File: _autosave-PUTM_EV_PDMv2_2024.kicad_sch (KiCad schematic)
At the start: 11 parts, among them J5 FTSH-107-01-L-DV-K-A, J6 USB_B_Micro, J7 USB_C_Receptacle_USB2.0_14P, U1 STM32G0C1KCTxN

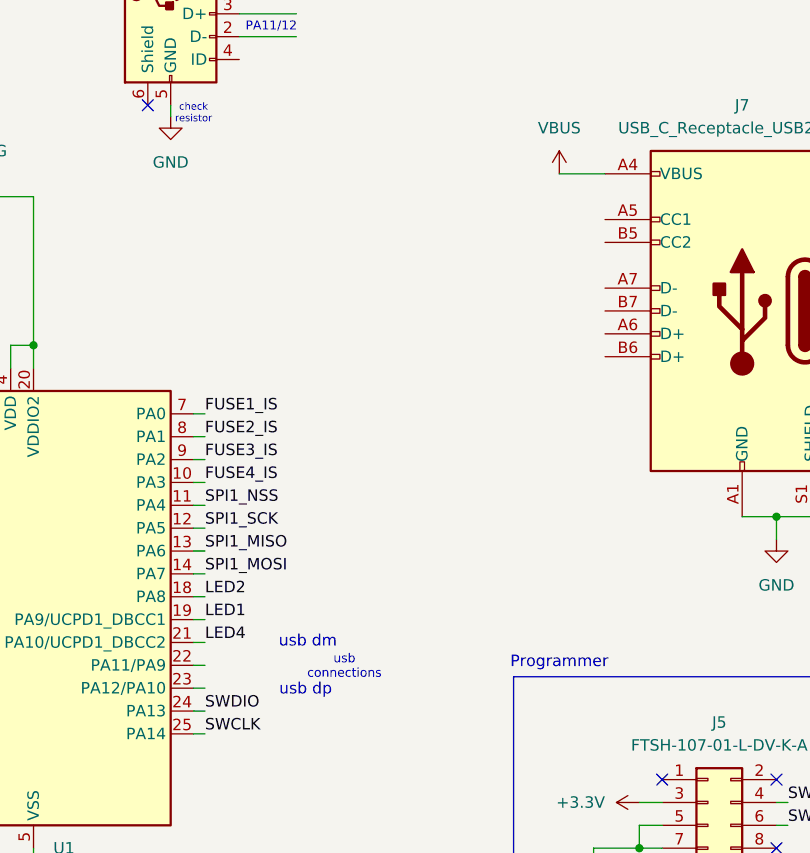
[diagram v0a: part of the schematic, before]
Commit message: Finished schematic
Added UCB C connection
Added CAN
Power ICs schematic fixed
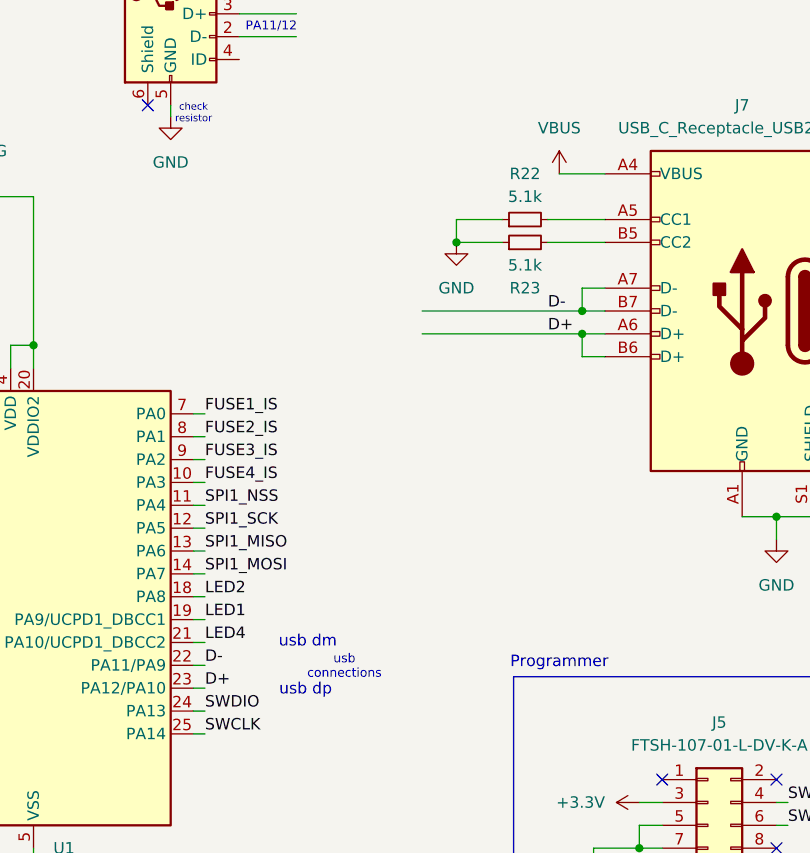
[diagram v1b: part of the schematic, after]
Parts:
- added R22, R23: 5.1k, symbol Device:R_Small
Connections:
- net GND: now also R22.1, R23.1
- net at J7.A5 (CC1): now also R22.2
- net D+: now reaches J7.A6 (D+)
- net D+: now also J7.B6 (D+), U1.23 (PA12/PA10)
- net D-: now reaches J7.A7 (D-)
- net D-: now also J7.B7 (D-), U1.22 (PA11/PA9)
- net at J7.B5 (CC2): now also R23.2
